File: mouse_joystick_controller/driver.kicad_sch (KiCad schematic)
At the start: 13 parts, among them J1 Conn_FFC_20_Pin_1mm_bottom-ZF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, U1 LVDS_4-4_HALF_DS91M040TSQE, U2 LVDS_4-4_HALF_DS91M040TSQE

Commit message: Add some sheets
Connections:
- net +3.3V: now also U1.10 (MDE), U2.10 (MDE), U2.16 (DE3), U2.25 (DE0)
- net GND: now also U2.13 (~{RE2}), U2.28 (~{RE1}), U2.4 (DI1), U2.6 (DI2)
- net POWER_ENABLE: now also U2.8 (DI3)
- net ~{DRIVER_ENABLE}: now also U2.2 (DI0)
- net REF: now reaches U2.3 (RO1)
- net REFR: now reaches U2.5 (RO2)
- no-connect marks 6 -> 16

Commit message: Add power jack
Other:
- moved on the sheet: C4, J1, R1, R2, R3, R4, R5, R6, R7, R8

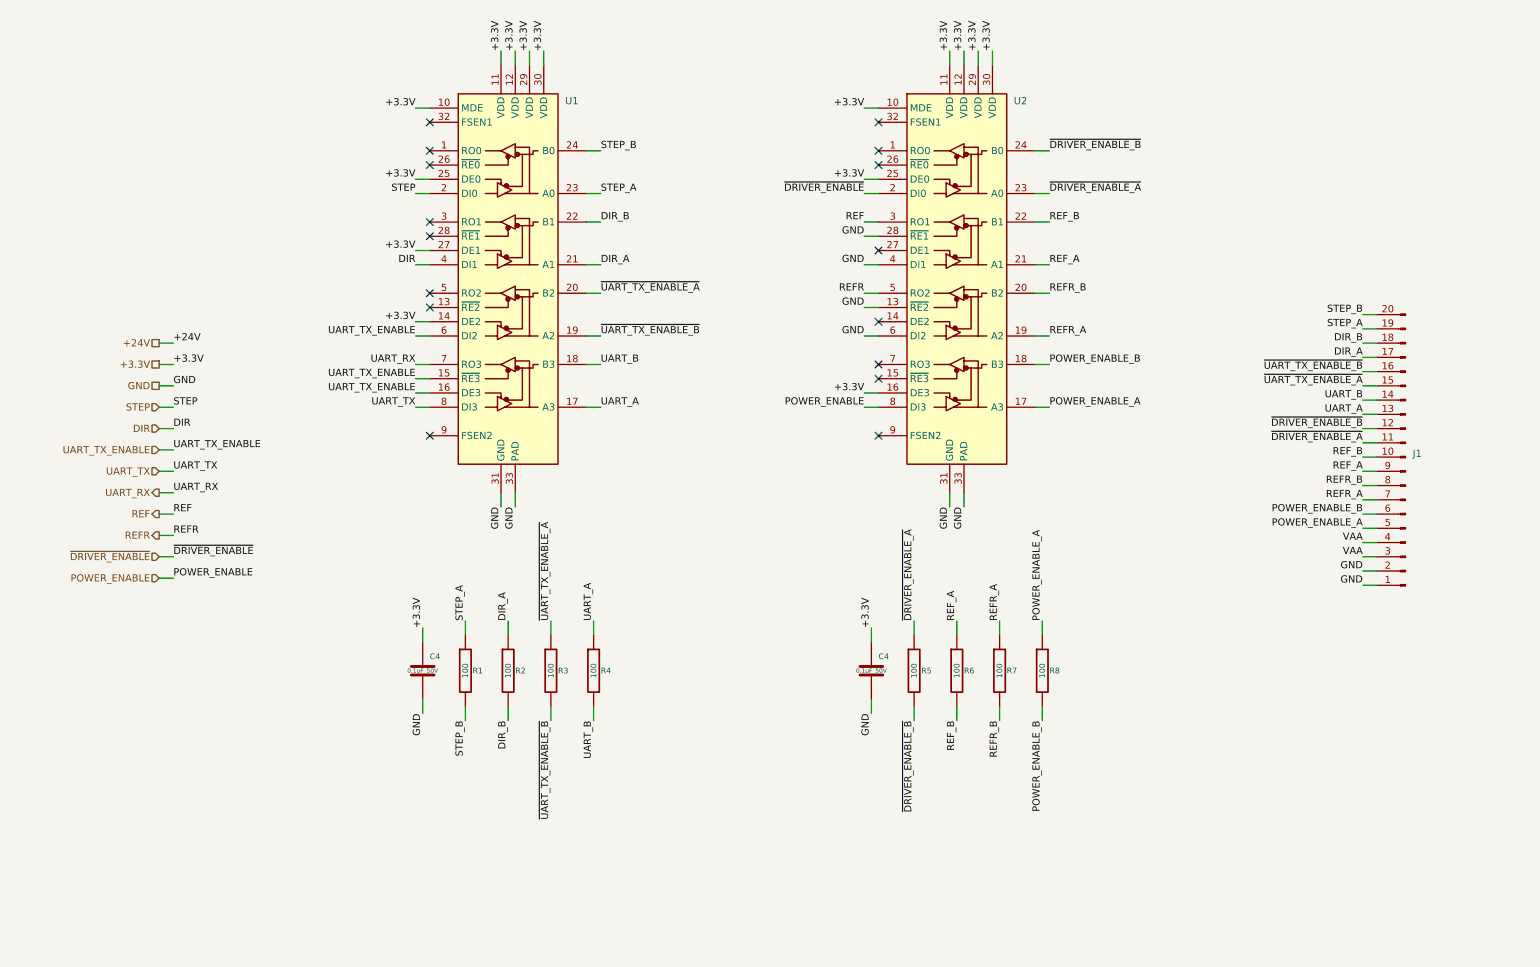
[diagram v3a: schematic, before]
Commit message: Rearrange sheets
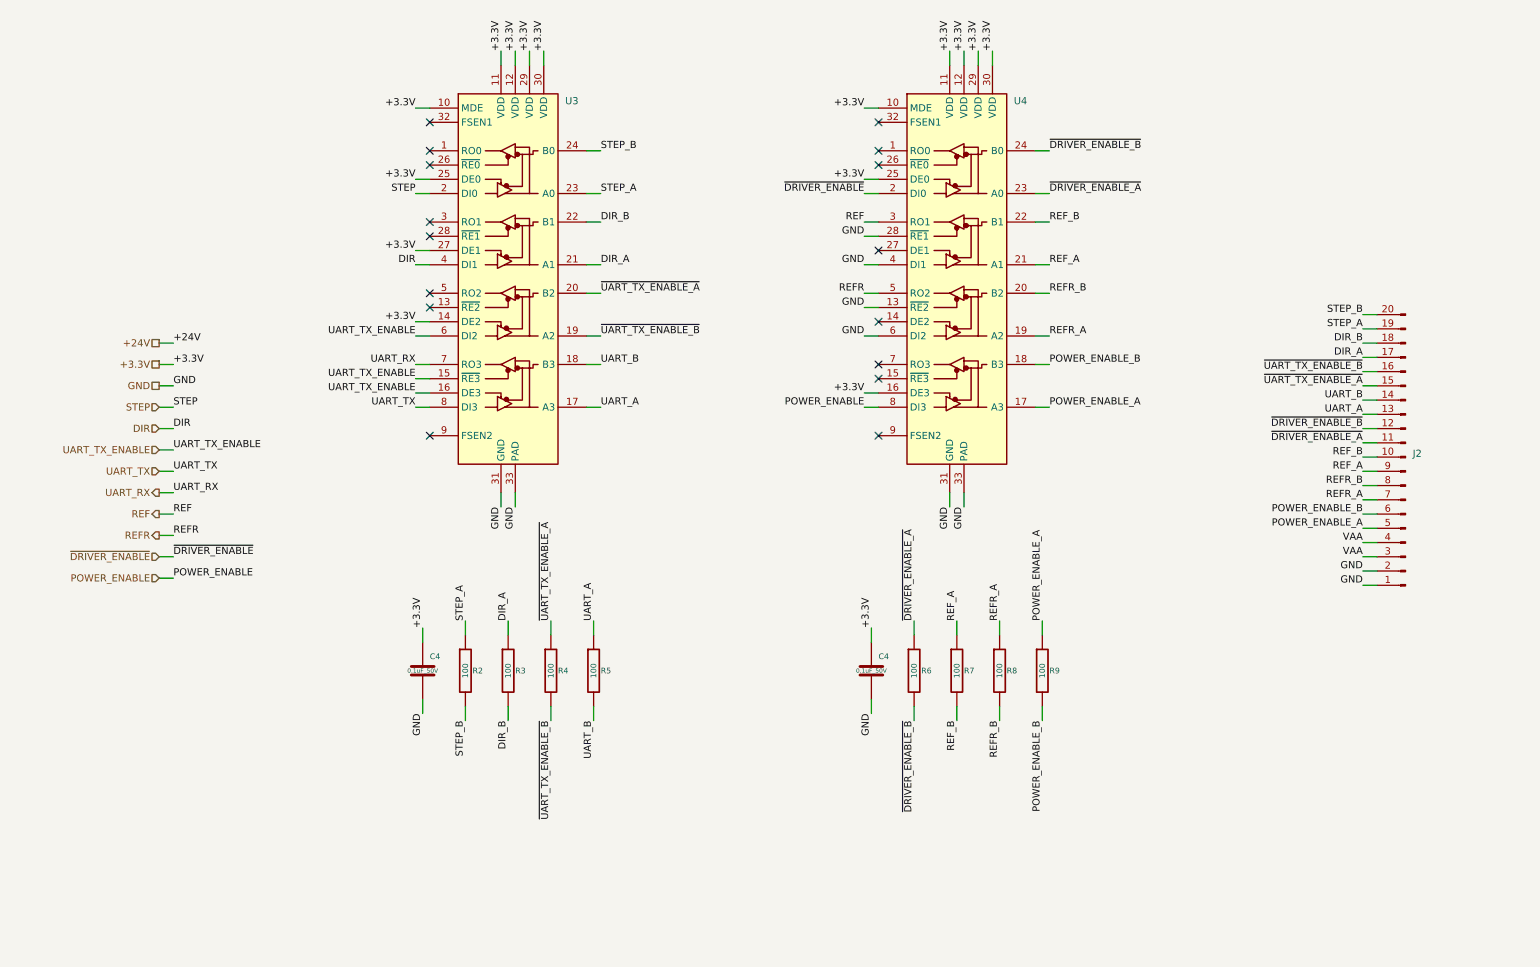
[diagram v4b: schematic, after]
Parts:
- renumbered J1 to J2, R1 to R2, R2 to R3, R3 to R4, R4 to R5, R5 to R6, R6 to R7, R7 to R8, R8 to R9, U1 to U3, U2 to U4
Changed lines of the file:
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@@
   (title_block
     (title "mouse_joystick_controller")
-    (date "2023-05-22")
+    (date "2023-05-24")
     (rev "2.0")
     (company "Howard Hughes Medical Institute")
@@
   (symbol (lib_id "Janelia:Conn_FFC_20_Pin_1mm_bottom-ZF1-20-01-T-WT-TR") (at 259.08 99.06 180) (unit 1)
     (in_bom yes) (on_board yes) (dnp no) (fields_autoplaced)
-    (property "Reference" "J1" (at 260.35 98.425 0)
+    (property "Reference" "J2" (at 260.35 98.425 0)
       (effects (font (size 1.27 1.27)) (justify right))
     )
@@
     (instances
       (project "mouse_joystick_controller"
-        (path "/cc457ebc-4af6-4663-b19f-8cb38f061cb4/77f41494-26e9-423c-a938-65116f1e9cbf"
-          (reference "J1") (unit 1)
+        (path "/cc457ebc-4af6-4663-b19f-8cb38f061cb4/3f8159dc-67a5-444d-b436-868704b45f22/00ddb26d-3c3d-4d0a-ba57-4e869ccb03df"
+          (reference "J2") (unit 1)
         )
       )
@@
   (symbol (lib_id "Janelia:LVDS_4-4_HALF_DS91M040TSQE") (at 99.06 67.31 0) (unit 1)
     (in_bom yes) (on_board yes) (dnp no) (fields_autoplaced)
-    (property "Reference" "U1" (at 109.22 35.56 0) (do_not_autoplace)
+    (property "Reference" "U3" (at 109.22 35.56 0) (do_not_autoplace)
       (effects (font (size 1.27 1.27)) (justify left))
     )
@@
     (instances
       (project "mouse_joystick_controller"
-        (path "/cc457ebc-4af6-4663-b19f-8cb38f061cb4/77f41494-26e9-423c-a938-65116f1e9cbf"
-          (reference "U1") (unit 1)
+        (path "/cc457ebc-4af6-4663-b19f-8cb38f061cb4/3f8159dc-67a5-444d-b436-868704b45f22/00ddb26d-3c3d-4d0a-ba57-4e869ccb03df"
+          (reference "U3") (unit 1)
         )
       )
@@
   (symbol (lib_id "Janelia:R_100_0402") (at 171.45 137.16 0) (unit 1)
     (in_bom yes) (on_board yes) (dnp no)
-    (property "Reference" "R5" (at 172.72 137.16 0)
+    (property "Reference" "R6" (at 172.72 137.16 0)
       (effects (font (size 1.016 1.016)) (justify left))
     )
@@
     (instances
       (project "mouse_joystick_controller"
-        (path "/cc457ebc-4af6-4663-b19f-8cb38f061cb4/77f41494-26e9-423c-a938-65116f1e9cbf"
-          (reference "R5") (unit 1)
+        (path "/cc457ebc-4af6-4663-b19f-8cb38f061cb4/3f8159dc-67a5-444d-b436-868704b45f22/00ddb26d-3c3d-4d0a-ba57-4e869ccb03df"
+          (reference "R6") (unit 1)
         )
       )
@@
   (symbol (lib_id "Janelia:R_100_0402") (at 186.69 137.16 0) (unit 1)
     (in_bom yes) (on_board yes) (dnp no)
-    (property "Reference" "R7" (at 187.96 137.16 0)
+    (property "Reference" "R8" (at 187.96 137.16 0)
       (effects (font (size 1.016 1.016)) (justify left))
     )
@@
     (instances
       (project "mouse_joystick_controller"
-        (path "/cc457ebc-4af6-4663-b19f-8cb38f061cb4/77f41494-26e9-423c-a938-65116f1e9cbf"
-          (reference "R7") (unit 1)
+        (path "/cc457ebc-4af6-4663-b19f-8cb38f061cb4/3f8159dc-67a5-444d-b436-868704b45f22/00ddb26d-3c3d-4d0a-ba57-4e869ccb03df"
+          (reference "R8") (unit 1)
         )
       )
@@
           (reference "C4") (unit 1)
         )
-        (path "/cc457ebc-4af6-4663-b19f-8cb38f061cb4/77f41494-26e9-423c-a938-65116f1e9cbf"
-          (reference "C1") (unit 1)
+        (path "/cc457ebc-4af6-4663-b19f-8cb38f061cb4/3f8159dc-67a5-444d-b436-868704b45f22/00ddb26d-3c3d-4d0a-ba57-4e869ccb03df"
+          (reference "C3") (unit 1)
         )
       )
@@
   (symbol (lib_id "Janelia:R_100_0402") (at 91.44 137.16 0) (unit 1)
     (in_bom yes) (on_board yes) (dnp no)
-    (property "Reference" "R1" (at 92.71 137.16 0)
+    (property "Reference" "R2" (at 92.71 137.16 0)
       (effects (font (size 1.016 1.016)) (justify left))
     )
@@
     (instances
       (project "mouse_joystick_controller"
-        (path "/cc457ebc-4af6-4663-b19f-8cb38f061cb4/77f41494-26e9-423c-a938-65116f1e9cbf"
-          (reference "R1") (unit 1)
+        (path "/cc457ebc-4af6-4663-b19f-8cb38f061cb4/3f8159dc-67a5-444d-b436-868704b45f22/00ddb26d-3c3d-4d0a-ba57-4e869ccb03df"
+          (reference "R2") (unit 1)
         )
       )
@@
           (reference "C4") (unit 1)
         )
-        (path "/cc457ebc-4af6-4663-b19f-8cb38f061cb4/77f41494-26e9-423c-a938-65116f1e9cbf"
-          (reference "C2") (unit 1)
+        (path "/cc457ebc-4af6-4663-b19f-8cb38f061cb4/3f8159dc-67a5-444d-b436-868704b45f22/00ddb26d-3c3d-4d0a-ba57-4e869ccb03df"
+          (reference "C4") (unit 1)
         )
       )
@@
   (symbol (lib_id "Janelia:LVDS_4-4_HALF_DS91M040TSQE") (at 179.07 67.31 0) (unit 1)
     (in_bom yes) (on_board yes) (dnp no) (fields_autoplaced)
-    (property "Reference" "U2" (at 189.23 35.56 0) (do_not_autoplace)
+    (property "Reference" "U4" (at 189.23 35.56 0) (do_not_autoplace)
       (effects (font (size 1.27 1.27)) (justify left))
     )
@@
     (instances
       (project "mouse_joystick_controller"
-        (path "/cc457ebc-4af6-4663-b19f-8cb38f061cb4/77f41494-26e9-423c-a938-65116f1e9cbf"
-          (reference "U2") (unit 1)
+        (path "/cc457ebc-4af6-4663-b19f-8cb38f061cb4/3f8159dc-67a5-444d-b436-868704b45f22/00ddb26d-3c3d-4d0a-ba57-4e869ccb03df"
+          (reference "U4") (unit 1)
         )
       )
@@
   (symbol (lib_id "Janelia:R_100_0402") (at 106.68 137.16 0) (unit 1)
     (in_bom yes) (on_board yes) (dnp no)
-    (property "Reference" "R3" (at 107.95 137.16 0)
+    (property "Reference" "R4" (at 107.95 137.16 0)
       (effects (font (size 1.016 1.016)) (justify left))
     )
@@
     (instances
       (project "mouse_joystick_controller"
-        (path "/cc457ebc-4af6-4663-b19f-8cb38f061cb4/77f41494-26e9-423c-a938-65116f1e9cbf"
-          (reference "R3") (unit 1)
+        (path "/cc457ebc-4af6-4663-b19f-8cb38f061cb4/3f8159dc-67a5-444d-b436-868704b45f22/00ddb26d-3c3d-4d0a-ba57-4e869ccb03df"
+          (reference "R4") (unit 1)
         )
       )
@@
   (symbol (lib_id "Janelia:R_100_0402") (at 179.07 137.16 0) (unit 1)
     (in_bom yes) (on_board yes) (dnp no)
-    (property "Reference" "R6" (at 180.34 137.16 0)
+    (property "Reference" "R7" (at 180.34 137.16 0)
       (effects (font (size 1.016 1.016)) (justify left))
     )
@@
     (instances
       (project "mouse_joystick_controller"
-        (path "/cc457ebc-4af6-4663-b19f-8cb38f061cb4/77f41494-26e9-423c-a938-65116f1e9cbf"
-          (reference "R6") (unit 1)
+        (path "/cc457ebc-4af6-4663-b19f-8cb38f061cb4/3f8159dc-67a5-444d-b436-868704b45f22/00ddb26d-3c3d-4d0a-ba57-4e869ccb03df"
+          (reference "R7") (unit 1)
         )
       )
@@
   (symbol (lib_id "Janelia:R_100_0402") (at 99.06 137.16 0) (unit 1)
     (in_bom yes) (on_board yes) (dnp no)
-    (property "Reference" "R2" (at 100.33 137.16 0)
+    (property "Reference" "R3" (at 100.33 137.16 0)
       (effects (font (size 1.016 1.016)) (justify left))
     )
@@
     (instances
       (project "mouse_joystick_controller"
-        (path "/cc457ebc-4af6-4663-b19f-8cb38f061cb4/77f41494-26e9-423c-a938-65116f1e9cbf"
-          (reference "R2") (unit 1)
+        (path "/cc457ebc-4af6-4663-b19f-8cb38f061cb4/3f8159dc-67a5-444d-b436-868704b45f22/00ddb26d-3c3d-4d0a-ba57-4e869ccb03df"
+          (reference "R3") (unit 1)
         )
       )
@@
   (symbol (lib_id "Janelia:R_100_0402") (at 194.31 137.16 0) (unit 1)
     (in_bom yes) (on_board yes) (dnp no)
-    (property "Reference" "R8" (at 195.58 137.16 0)
+    (property "Reference" "R9" (at 195.58 137.16 0)
       (effects (font (size 1.016 1.016)) (justify left))
     )
@@
     (instances
       (project "mouse_joystick_controller"
-        (path "/cc457ebc-4af6-4663-b19f-8cb38f061cb4/77f41494-26e9-423c-a938-65116f1e9cbf"
-          (reference "R8") (unit 1)
+        (path "/cc457ebc-4af6-4663-b19f-8cb38f061cb4/3f8159dc-67a5-444d-b436-868704b45f22/00ddb26d-3c3d-4d0a-ba57-4e869ccb03df"
+          (reference "R9") (unit 1)
         )
       )
@@
   (symbol (lib_id "Janelia:R_100_0402") (at 114.3 137.16 0) (unit 1)
     (in_bom yes) (on_board yes) (dnp no)
-    (property "Reference" "R4" (at 115.57 137.16 0)
+    (property "Reference" "R5" (at 115.57 137.16 0)
       (effects (font (size 1.016 1.016)) (justify left))
     )
@@
     (instances
       (project "mouse_joystick_controller"
-        (path "/cc457ebc-4af6-4663-b19f-8cb38f061cb4/77f41494-26e9-423c-a938-65116f1e9cbf"
-          (reference "R4") (unit 1)
+        (path "/cc457ebc-4af6-4663-b19f-8cb38f061cb4/3f8159dc-67a5-444d-b436-868704b45f22/00ddb26d-3c3d-4d0a-ba57-4e869ccb03df"
+          (reference "R5") (unit 1)
         )
       )

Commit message: Add DDS chip in audio sheet
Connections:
- net VAA is gone; now on net +24V: J2.3 (Pin_3), J2.4 (Pin_4)
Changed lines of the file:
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@@
   (title_block
     (title "mouse_joystick_controller")
-    (date "2023-06-02")
+    (date "2023-06-06")
     (rev "2.0")
     (company "Howard Hughes Medical Institute")
@@
     (effects (font (size 1.27 1.27)) (justify left bottom))
   )
-  (label "VAA" (at 251.46 114.3 180) (fields_autoplaced)
-    (effects (font (size 1.27 1.27)) (justify right bottom))
-  )
   (label "STEP_B" (at 91.44 146.05 270) (fields_autoplaced)
     (effects (font (size 1.27 1.27)) (justify right bottom))
@@
     (effects (font (size 1.27 1.27)) (justify left bottom))
   )
+  (label "+24V" (at 251.46 116.84 180) (fields_autoplaced)
+    (effects (font (size 1.27 1.27)) (justify right bottom))
+  )
   (label "~{UART_TX_ENABLE_B}" (at 115.57 77.47 0) (fields_autoplaced)
     (effects (font (size 1.27 1.27)) (justify left bottom))
@@
     (effects (font (size 1.27 1.27)) (justify right bottom))
   )
-  (label "VAA" (at 251.46 116.84 180) (fields_autoplaced)
-    (effects (font (size 1.27 1.27)) (justify right bottom))
-  )
   (label "+3.3V" (at 82.55 74.93 180) (fields_autoplaced)
     (effects (font (size 1.27 1.27)) (justify right bottom))
@@
     (effects (font (size 1.27 1.27)) (justify right bottom))
   )
+  (label "+24V" (at 251.46 114.3 180) (fields_autoplaced)
+    (effects (font (size 1.27 1.27)) (justify right bottom))
+  )

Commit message: power_enable -> standby
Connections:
- net POWER_ENABLE renamed STANDBY
- net POWER_ENABLE_A renamed STANDBY_A
- net POWER_ENABLE_B renamed STANDBY_B
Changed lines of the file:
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@@
   (title_block
     (title "mouse_joystick_controller")
-    (date "2023-06-06")
+    (date "2023-06-07")
     (rev "2.0")
     (company "Howard Hughes Medical Institute")
@@
     (effects (font (size 1.27 1.27)) (justify left bottom))
   )
-  (label "POWER_ENABLE_A" (at 195.58 90.17 0) (fields_autoplaced)
+  (label "STANDBY_A" (at 195.58 90.17 0) (fields_autoplaced)
     (effects (font (size 1.27 1.27)) (justify left bottom))
   )
@@
     (effects (font (size 1.27 1.27)) (justify right bottom))
   )
-  (label "POWER_ENABLE_B" (at 251.46 109.22 180) (fields_autoplaced)
+  (label "STANDBY_B" (at 251.46 109.22 180) (fields_autoplaced)
     (effects (font (size 1.27 1.27)) (justify right bottom))
   )
@@
     (effects (font (size 1.27 1.27)) (justify right bottom))
   )
-  (label "POWER_ENABLE_B" (at 194.31 146.05 270) (fields_autoplaced)
+  (label "STANDBY_B" (at 194.31 146.05 270) (fields_autoplaced)
     (effects (font (size 1.27 1.27)) (justify right bottom))
   )
@@
     (effects (font (size 1.27 1.27)) (justify right bottom))
   )
-  (label "POWER_ENABLE_A" (at 194.31 128.27 90) (fields_autoplaced)
+  (label "STANDBY_A" (at 194.31 128.27 90) (fields_autoplaced)
     (effects (font (size 1.27 1.27)) (justify left bottom))
   )
@@
     (effects (font (size 1.27 1.27)) (justify right bottom))
   )
-  (label "POWER_ENABLE_A" (at 251.46 111.76 180) (fields_autoplaced)
+  (label "STANDBY_A" (at 251.46 111.76 180) (fields_autoplaced)
     (effects (font (size 1.27 1.27)) (justify right bottom))
   )
@@
     (effects (font (size 1.27 1.27)) (justify left bottom))
   )
-  (label "POWER_ENABLE" (at 162.56 90.17 180) (fields_autoplaced)
+  (label "STANDBY" (at 162.56 90.17 180) (fields_autoplaced)
     (effects (font (size 1.27 1.27)) (justify right bottom))
   )
@@
     (effects (font (size 1.27 1.27)) (justify right bottom))
   )
-  (label "POWER_ENABLE_B" (at 195.58 82.55 0) (fields_autoplaced)
+  (label "STANDBY_B" (at 195.58 82.55 0) (fields_autoplaced)
     (effects (font (size 1.27 1.27)) (justify left bottom))
   )
@@
     (effects (font (size 1.27 1.27)) (justify left bottom))
   )
-  (label "POWER_ENABLE" (at 39.37 120.65 0) (fields_autoplaced)
+  (label "STANDBY" (at 39.37 120.65 0) (fields_autoplaced)
     (effects (font (size 1.27 1.27)) (justify left bottom))
   )
@@
     (effects (font (size 1.27 1.27)) (justify left bottom))
   )
-  (hierarchical_label "POWER_ENABLE" (shape input) (at 36.83 120.65 180) (fields_autoplaced)
+  (hierarchical_label "STANDBY" (shape input) (at 36.83 120.65 180) (fields_autoplaced)
     (effects (font (size 1.27 1.27)) (justify right))
   )

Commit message: Test pin rcpt
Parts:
- renumbered J2 to J4, U3 to U6, U4 to U7
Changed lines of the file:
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@@
   (title_block
     (title "mouse_joystick_controller")
-    (date "2023-06-07")
+    (date "2023-06-09")
     (rev "2.0")
     (company "Howard Hughes Medical Institute")
@@
   (symbol (lib_id "Janelia:Conn_FFC_20_Pin_1mm_bottom-ZF1-20-01-T-WT-TR") (at 259.08 99.06 180) (unit 1)
     (in_bom yes) (on_board yes) (dnp no) (fields_autoplaced)
-    (property "Reference" "J2" (at 260.35 98.425 0)
+    (property "Reference" "J4" (at 260.35 97.79 0)
       (effects (font (size 1.27 1.27)) (justify right))
     )
@@
     )
     (property "Vendor Part Number" "SAM14906CT-ND" (at 259.08 130.81 0)
+      (effects (font (size 1.27 1.27)) hide)
+    )
+    (property "Sim.Enable" "0" (at 259.08 99.06 0)
       (effects (font (size 1.27 1.27)) hide)
     )
@@
       (project "mouse_joystick_controller"
         (path "/cc457ebc-4af6-4663-b19f-8cb38f061cb4/3f8159dc-67a5-444d-b436-868704b45f22/00ddb26d-3c3d-4d0a-ba57-4e869ccb03df"
-          (reference "J2") (unit 1)
+          (reference "J4") (unit 1)
         )
       )
@@
   (symbol (lib_id "Janelia:LVDS_4-4_HALF_DS91M040TSQE") (at 99.06 67.31 0) (unit 1)
     (in_bom yes) (on_board yes) (dnp no) (fields_autoplaced)
-    (property "Reference" "U3" (at 109.22 35.56 0) (do_not_autoplace)
+    (property "Reference" "U6" (at 109.22 35.56 0) (do_not_autoplace)
       (effects (font (size 1.27 1.27)) (justify left))
     )
@@
     )
     (property "Vendor Part Number" "DS91M040TSQE/NOPBCT-ND" (at 99.06 16.51 0)
+      (effects (font (size 1.27 1.27)) hide)
+    )
+    (property "Sim.Enable" "0" (at 99.06 67.31 0)
       (effects (font (size 1.27 1.27)) hide)
     )
@@
       (project "mouse_joystick_controller"
         (path "/cc457ebc-4af6-4663-b19f-8cb38f061cb4/3f8159dc-67a5-444d-b436-868704b45f22/00ddb26d-3c3d-4d0a-ba57-4e869ccb03df"
-          (reference "U3") (unit 1)
+          (reference "U6") (unit 1)
         )
       )
@@
         )
         (path "/cc457ebc-4af6-4663-b19f-8cb38f061cb4/3f8159dc-67a5-444d-b436-868704b45f22/00ddb26d-3c3d-4d0a-ba57-4e869ccb03df"
-          (reference "C3") (unit 1)
+          (reference "C5") (unit 1)
         )
       )
@@
         )
         (path "/cc457ebc-4af6-4663-b19f-8cb38f061cb4/3f8159dc-67a5-444d-b436-868704b45f22/00ddb26d-3c3d-4d0a-ba57-4e869ccb03df"
-          (reference "C4") (unit 1)
+          (reference "C6") (unit 1)
         )
       )
@@
   (symbol (lib_id "Janelia:LVDS_4-4_HALF_DS91M040TSQE") (at 179.07 67.31 0) (unit 1)
     (in_bom yes) (on_board yes) (dnp no) (fields_autoplaced)
-    (property "Reference" "U4" (at 189.23 35.56 0) (do_not_autoplace)
+    (property "Reference" "U7" (at 189.23 35.56 0) (do_not_autoplace)
       (effects (font (size 1.27 1.27)) (justify left))
     )
@@
     )
     (property "Vendor Part Number" "DS91M040TSQE/NOPBCT-ND" (at 179.07 16.51 0)
+      (effects (font (size 1.27 1.27)) hide)
+    )
+    (property "Sim.Enable" "0" (at 179.07 67.31 0)
       (effects (font (size 1.27 1.27)) hide)
     )
@@
       (project "mouse_joystick_controller"
         (path "/cc457ebc-4af6-4663-b19f-8cb38f061cb4/3f8159dc-67a5-444d-b436-868704b45f22/00ddb26d-3c3d-4d0a-ba57-4e869ccb03df"
-          (reference "U4") (unit 1)
+          (reference "U7") (unit 1)
         )
       )
